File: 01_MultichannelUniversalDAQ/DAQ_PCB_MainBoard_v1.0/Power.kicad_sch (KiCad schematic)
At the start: 86 parts, among them J1 Molex 1x2, J2 Pin Header 1x6, Q1 SQ2337CES, Q2 SQ2337CES, U1 REF5050, U2 NCV8182C, U3 NCV8182C, U4 NCV8182C, U5 DPBW06, U6 SPBW06

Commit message: Commit after meeting
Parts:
- added C79: 100n, Capacitor_SMD:C_0603_1608Metric_Pad1.08x0.95mm_HandSolder, symbol Device:C_Small
- added L8: MPZ2012S601AT000, Inductor_SMD:L_0805_2012Metric_Pad1.05x1.20mm_HandSolder, symbol KJ_KiCadLib:Ferrite_Bead
- added R33, R97: 0R, Resistor_SMD:R_0603_1608Metric_Pad0.98x0.95mm_HandSolder, symbol Device:R_Small
- added R95, R96: 10k, Resistor_SMD:R_0603_1608Metric_Pad0.98x0.95mm_HandSolder, symbol Device:R_Small
- added TP25: TestPoint, TestPoint:TestPoint_Pad_D1.0mm, symbol Connector:TestPoint
- added U17: OPA2197, Package_SO:SOIC-8_3.9x4.9mm_P1.27mm, symbol Amplifier_Operational:OPA2197xD
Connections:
- net 5V: now also C79.1, R97.1, U17.8 (V+)
- net 5Vref: now also R33.1
- net GND: now also C79.2, L8.2, R96.2, U17.4 (V-)
- net at C24.2, C25.1, C27.2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: now also L8.1
- new net: R33.2, R95.1, R97.2
- new net: R95.2, R96.1, U17.3 (+)
- new net: U17.5 (+), U17.6 (-), U17.7
- new net ADC_0: TP25.1, U17.1, U17.2 (-)

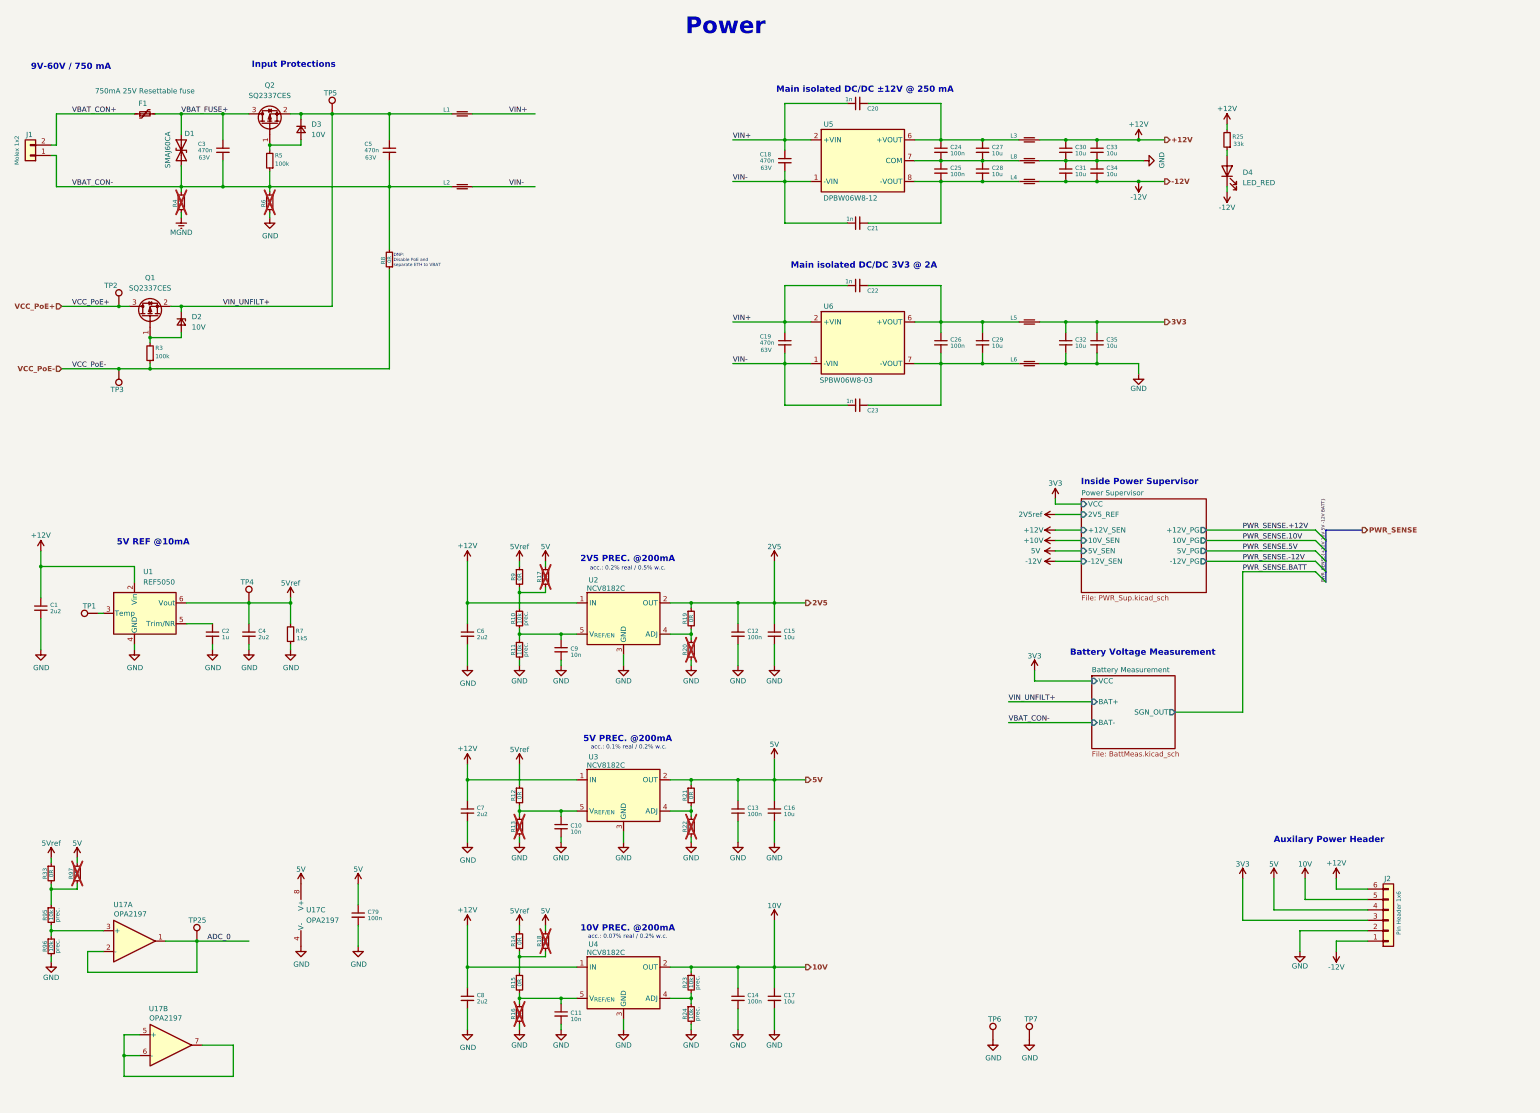
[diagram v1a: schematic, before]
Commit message: New power concept begin
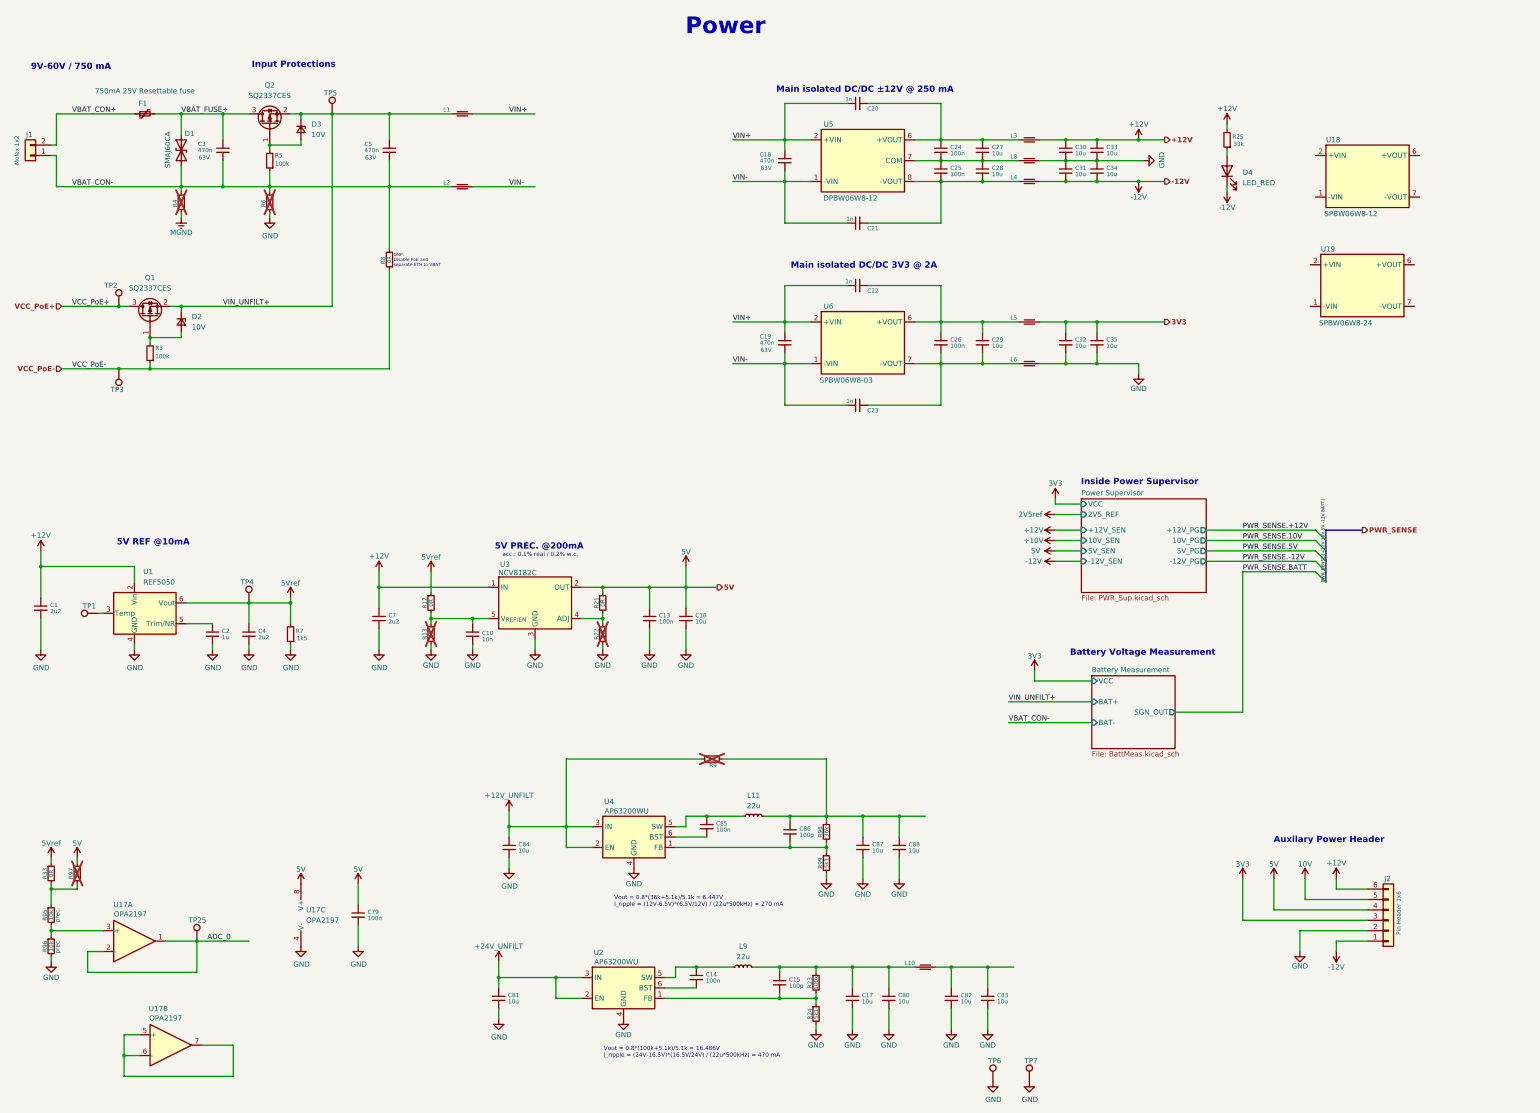
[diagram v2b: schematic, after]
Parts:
- removed C11, C9: 10n, Capacitor_SMD:C_0603_1608Metric_Pad1.08x0.95mm_HandSolder, symbol Device:C_Small
- removed C12: 100n, Capacitor_SMD:C_0603_1608Metric_Pad1.08x0.95mm_HandSolder, symbol Device:C_Small
- removed C6, C8: 2u2, Capacitor_SMD:C_0805_2012Metric_Pad1.18x1.45mm_HandSolder, symbol Device:C_Small
- removed R10, R11: 10k, Resistor_SMD:R_0603_1608Metric_Pad0.98x0.95mm_HandSolder, symbol Device:R_Small
- removed R14, R15, R16, R17, R18, R19, R20: 0R, Resistor_SMD:R_0603_1608Metric_Pad0.98x0.95mm_HandSolder, symbol Device:R_Small
- removed U2, U4: NCV8182C, Package_TO_SOT_SMD:TO-252-5_TabPin3, symbol KJ_KiCadLib:NCV8182C
- added C80, C81, C82, C83, C84, C87, C88: 10u, Capacitor_SMD:C_1206_3216Metric_Pad1.33x1.80mm_HandSolder, symbol Device:C_Small
- added C85: 100n, Capacitor_SMD:C_0603_1608Metric_Pad1.08x0.95mm_HandSolder, symbol Device:C_Small
- added C86: 100p, Capacitor_SMD:C_0603_1608Metric_Pad1.08x0.95mm_HandSolder, symbol Device:C_Small
- added L10: MPZ2012S601AT000, Inductor_SMD:L_0805_2012Metric_Pad1.05x1.20mm_HandSolder, symbol KJ_KiCadLib:Ferrite_Bead
- added L11, L9: 22u, symbol Device:L_Small
- added R98: 36k, Resistor_SMD:R_0603_1608Metric_Pad0.98x0.95mm_HandSolder, symbol Device:R_Small
- added R99: 5k1, Resistor_SMD:R_0603_1608Metric_Pad0.98x0.95mm_HandSolder, symbol Device:R_Small
- added U18, U19: SPBW06, KJ_KiCadLib_ICs:SPBW03_DPBW03, symbol KJ_KiCadLib:SPBW03F
- added U2, U4: AP63200WU, Package_TO_SOT_SMD:TSOT-23-6, symbol Regulator_Switching:AP63200WU
- C15: value 10u -> 100p; footprint Capacitor_SMD:C_1206_3216Metric_Pad1.33x1.80mm_HandSolder -> Capacitor_SMD:C_0603_1608Metric_Pad1.08x0.95mm_HandSolder
- R23: value 10k -> 100k; Precision prec. -> (none)
- R24: value 10k -> 5k1; Precision prec. -> (none)
- R9: footprint Resistor_SMD:R_0603_1608Metric_Pad0.98x0.95mm_HandSolder -> Resistor_SMD:R_1206_3216Metric_Pad1.30x1.75mm_HandSolder; now not fitted
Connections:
- net 10V: no longer C14.1, C17.1, R23.1
- net 5Vref: no longer R9.1
- net GND: now also C80.2, C81.2, C82.2, C83.2, C84.2, C87.2, C88.2, R99.2, U2.4 (GND), U4.4 (GND); no longer C14.2, C15.2
- net at R23.2, R24.1: now also C15.2, U2.1 (FB)
- net +12V_UNFILT: now reaches R9.2
- net +12V_UNFILT: now also C84.1, U4.2 (EN), U4.3 (IN)
- net 2V5: no longer names the net of C15.1
- net 2V5: now also C17.1, R23.1, C80.1, L10.1, L9.2
- new net: C82.1, C83.1, L10.2
- new net: U18.3 (NC), U18.5 (NC), U18.8 (NC)
- new net: C86.1, C87.1, C88.1, L11.2, R9.1, R98.1
- new net: C85.1, L11.1, U4.5 (SW)
- new net: C85.2, U4.6 (BST)
- new net: C86.2, R98.2, R99.1, U4.1 (FB)
- new net: U19.3 (NC), U19.5 (NC), U19.8 (NC)
- new net: C14.1, L9.1, U2.5 (SW)
- new net: C14.2, U2.6 (BST)
- new net +24V_UNFILT: C81.1, U2.2 (EN), U2.3 (IN)
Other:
- note added: "Vout = 0.8*(100k+5.1k)/5.1k = 16.486V I_ripple = (24V-16.5V)*(16.5V/24V) / (22u*500kHz) = 470 mA"
- note added: "Vout = 0.8*(36k+5.1k)/5.1k = 6.447V I_ripple = (12V-6.5V)*(6.5V/12V) / (22u*500kHz) = 270 mA"
- note removed: "10V PREC. @200mA"
- note removed: "2V5 PREC. @200mA"
- note removed: "acc.: 0.07% real / 0.2% w.c."
- note removed: "acc.: 0.2% real / 0.5% w.c."
- moved on the sheet: C10, C13, C16, C7, R12, R13, R21, R22, TP6, TP7, U3

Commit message: power in progress
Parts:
- removed L9: 22u, symbol Device:L_Small
- removed U4: AP63200WU, Package_TO_SOT_SMD:TSOT-23-6, symbol Regulator_Switching:AP63200WU
- added L12: 68u, Inductor_SMD:L_6.3x6.3_H3, symbol Device:L_Small
- added U20: LMR51630Y, Package_TO_SOT_SMD:SOT-23-6, symbol Regulator_Switching:LMR50410
- C86: value 100p -> 100n
- L11: value 22u -> 68u; footprint (none) -> Inductor_SMD:L_6.3x6.3_H3; Part Number (none) -> VLS6045EX-680M
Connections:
- net +12V_UNFILT: now also C86.1, U20.4 (EN), U20.5 (VIN)
- net GND: now also C86.2, U20.2 (GND)
- net at C87.1, C88.1, L11.2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: no longer C86.1
- net at C85.1: now also U20.1 (CB); no longer L11.1
- net at C85.2: now also L11.1, U20.6 (SW)
- net at R98.2, R99.1: now also U20.3 (FB); no longer C86.2
- net at C15.1, C17.1, C80.1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: now also L12.2
- net at C14.1, U2.5 (SW): now also L12.1
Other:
- note added: "Vout = 0.8*(100k+5.1k)/5.1k = 16.486V I_ripple = (24V-16.5V)*(16.5V/24V) / (68u*1.1MHz) = 70 mA"
- note added: "Vout = 0.8*(36k+5.1k)/5.1k = 6.447V I_ripple = (12V-6.5V)*(6.5V/12V) / (68u*1.1MHz) = 40 mA"
- note removed: "Vout = 0.8*(100k+5.1k)/5.1k = 16.486V I_ripple = (24V-16.5V)*(16.5V/24V) / (22u*500kHz) = 470 mA"
- note removed: "Vout = 0.8*(36k+5.1k)/5.1k = 6.447V I_ripple = (12V-6.5V)*(6.5V/12V) / (22u*500kHz) = 270 mA"
- moved on the sheet: C84, C87, C88, L11, R9, R98, R99

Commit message: new power concept
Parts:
- removed C13, C14, C79: 100n, Capacitor_SMD:C_0603_1608Metric_Pad1.08x0.95mm_HandSolder, symbol Device:C_Small
- removed C15: 100p, Capacitor_SMD:C_0603_1608Metric_Pad1.08x0.95mm_HandSolder, symbol Device:C_Small
- removed C17, C32, C33, C34, C35: 10u, Capacitor_SMD:C_1206_3216Metric_Pad1.33x1.80mm_HandSolder, symbol Device:C_Small
- removed C7: 2u2, Capacitor_SMD:C_0805_2012Metric_Pad1.18x1.45mm_HandSolder, symbol Device:C_Small
- removed J2: Pin Header 1x6, Connector_PinHeader_2.54mm:PinHeader_1x06_P2.54mm_Vertical, symbol Connector_Generic:Conn_01x06
- removed R23: 100k, Resistor_SMD:R_0603_1608Metric_Pad0.98x0.95mm_HandSolder, symbol Device:R_Small
- removed R95, R96: 10k, Resistor_SMD:R_0603_1608Metric_Pad0.98x0.95mm_HandSolder, symbol Device:R_Small
- removed R97: 0R, Resistor_SMD:R_0603_1608Metric_Pad0.98x0.95mm_HandSolder, symbol Device:R_Small
- removed TP25: TestPoint, TestPoint:TestPoint_Pad_D1.0mm, symbol Connector:TestPoint
- removed U17: OPA2197, Package_SO:SOIC-8_3.9x4.9mm_P1.27mm, symbol Amplifier_Operational:OPA2197xD
- removed U18: SPBW06, KJ_KiCadLib_ICs:SPBW03_DPBW03, symbol KJ_KiCadLib:SPBW03F
- removed U2: AP63200WU, Package_TO_SOT_SMD:TSOT-23-6, symbol Regulator_Switching:AP63200WU
- added C100, C101, C89, C92, C93, C94, C95, C97, C99: 10u, Capacitor_SMD:C_1206_3216Metric_Pad1.33x1.80mm_HandSolder, symbol Device:C_Small
- added C90, C91, C98: 100n, Capacitor_SMD:C_0603_1608Metric_Pad1.08x0.95mm_HandSolder, symbol Device:C_Small
- added C96: 1u, Capacitor_SMD:C_0603_1608Metric_Pad1.08x0.95mm_HandSolder, symbol Device:C_Small
- added D8: LED_RED, LED_SMD:LED_0805_2012Metric_Pad1.15x1.40mm_HandSolder, symbol Device:LED
- added J14: Pin Header 1x5, Connector_PinHeader_2.54mm:PinHeader_1x05_P2.54mm_Vertical, symbol Connector_Generic:Conn_01x05
- added L13, L14, L15, L9: MPZ2012S601AT000, Inductor_SMD:L_0805_2012Metric_Pad1.05x1.20mm_HandSolder, symbol KJ_KiCadLib:Ferrite_Bead
- added R101: 5k1, Resistor_SMD:R_0603_1608Metric_Pad0.98x0.95mm_HandSolder, symbol Device:R_Small
- added U21: LMR51630Y, Package_TO_SOT_SMD:SOT-23-6, symbol Regulator_Switching:LMR50410
- C20, C21, C22, C23: Voltage (none) -> 200V
- C24, C25, C27, C28, C30, C81, C83: Voltage (none) -> 50V
- C26: value 100n -> 1n; Voltage (none) -> 200V
- C29: value 10u -> 1n; footprint Capacitor_SMD:C_1206_3216Metric_Pad1.33x1.80mm_HandSolder -> Capacitor_SMD:C_0603_1608Metric_Pad1.08x0.95mm_HandSolder; Voltage (none) -> 200V
- C31: value 10u -> 470n; Part Number (none) -> C1206C474KMREC7210; Voltage (none) -> 63V
- C80: value 10u -> 100n; footprint Capacitor_SMD:C_1206_3216Metric_Pad1.33x1.80mm_HandSolder -> Capacitor_SMD:C_0603_1608Metric_Pad1.08x0.95mm_HandSolder; Voltage (none) -> 50V
- R24: value 5k1 -> 100k
- R25: value 33k -> 1k
- R33: value 0R -> 4k7
- U19: Part Number SPBW06W8-24 -> SPBW06W8-12
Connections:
- net +24V_UNFILT is gone; now on an unnamed net: C81.1
- net +12V: no longer C30.1, L3.2, R25.2, U3.1 (IN)
- net -12V: no longer C31.2, D4.1 (K), L4.2
- net 3V3: now also C100.1, C101.1, J14.2 (Pin_2)
- net 5V: now also R25.2, J14.3 (Pin_3)
- net 5Vref: no longer R33.1
- net GND: now also C28.2, D4.1 (K), L4.2, C100.2, C101.2, C89.2, C90.2, C92.2, C93.2, C94.2, C95.2, C96.2, C97.2, D8.1 (K), J14.1 (Pin_1), L9.2, R101.2, U21.2 (GND); no longer C31.1, C80.2, C81.2, L8.2, R24.2
- net VIN+: now also C26.1, C31.1, U19.2 (+VIN)
- net VIN-: now also C29.1, C31.2, U19.1 (-VIN)
- net 6V5: now reaches C82.1, L10.2
- net 6V5: now also U3.1 (IN), C96.1; no longer C83.1
- net 16V5: now reaches R33.2
- net 16V5: now also C94.1, C95.1, L13.2
- net at C87.1, C88.1, L11.2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: now also L10.1
- net at C24.2, C25.1, U5.7 (COM): no longer C27.2, C28.1, L8.1
- net at C21.2, C25.2, L4.1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: now also C27.2; no longer C28.2
- net at R24.1: now also L12.2, C92.1, C93.1, L13.1
- net at C29.2, L6.1, U6.7 (-VOUT): now also C98.2, C99.2; no longer C23.2, C26.2
- net at U19.6 (+VOUT): now also C22.2, C80.1, L8.1
- net at U19.7 (-VOUT): now also C23.2, C80.2, C81.2, L9.1
- net at L12.1: now also C91.2, U21.6 (SW)
- net +12V_UNFILT: no longer names the net of C84.1, C86.1, R9.2, U20.4 (EN), U20.5 (VIN)
- net +12V_UNFILT: now also L14.2
- new net: D8.2 (A), R33.1
- new net: C26.2, C98.1, C99.1, L5.1, U6.6 (+VOUT)
- new net: C91.1, U21.1 (CB)
- new net: R101.1, R24.2, U21.3 (FB)
- new net: C89.1, C90.1, L15.2, U21.4 (EN), U21.5 (VIN)
- new net 12V: C83.1, C97.1, J14.4 (Pin_4), L14.1, L8.2
- new net 24V: C28.1, C30.1, J14.5 (Pin_5), L15.1, L3.2
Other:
- note added: "16.5V @200mA"
- note added: "6.5V @200mA"
- note added: "Main isolated DC/DC 12V @250mA"
- note added: "Main isolated DC/DC 24V @250mA"
- note added: "Main isolated DC/DC 3V3 @ 1A"
- note added: "acc.: 0.03% real / 0.2% w.c."
- note removed: "Main isolated DC/DC 3V3 @ 2A"
- note removed: "Main isolated DC/DC ±12V @ 250 mA"
- note removed: "acc.: 0.1% real / 0.2% w.c."
- moved on the sheet: C10, C16, C18, C19, C20, C24, C82, C84, C85, C86, C87, C88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
